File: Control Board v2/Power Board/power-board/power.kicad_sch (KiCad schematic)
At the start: 14 parts, among them J1 1366005, J6 Conn_01x04, J7 Conn_01x02, SW1 SW_SPST

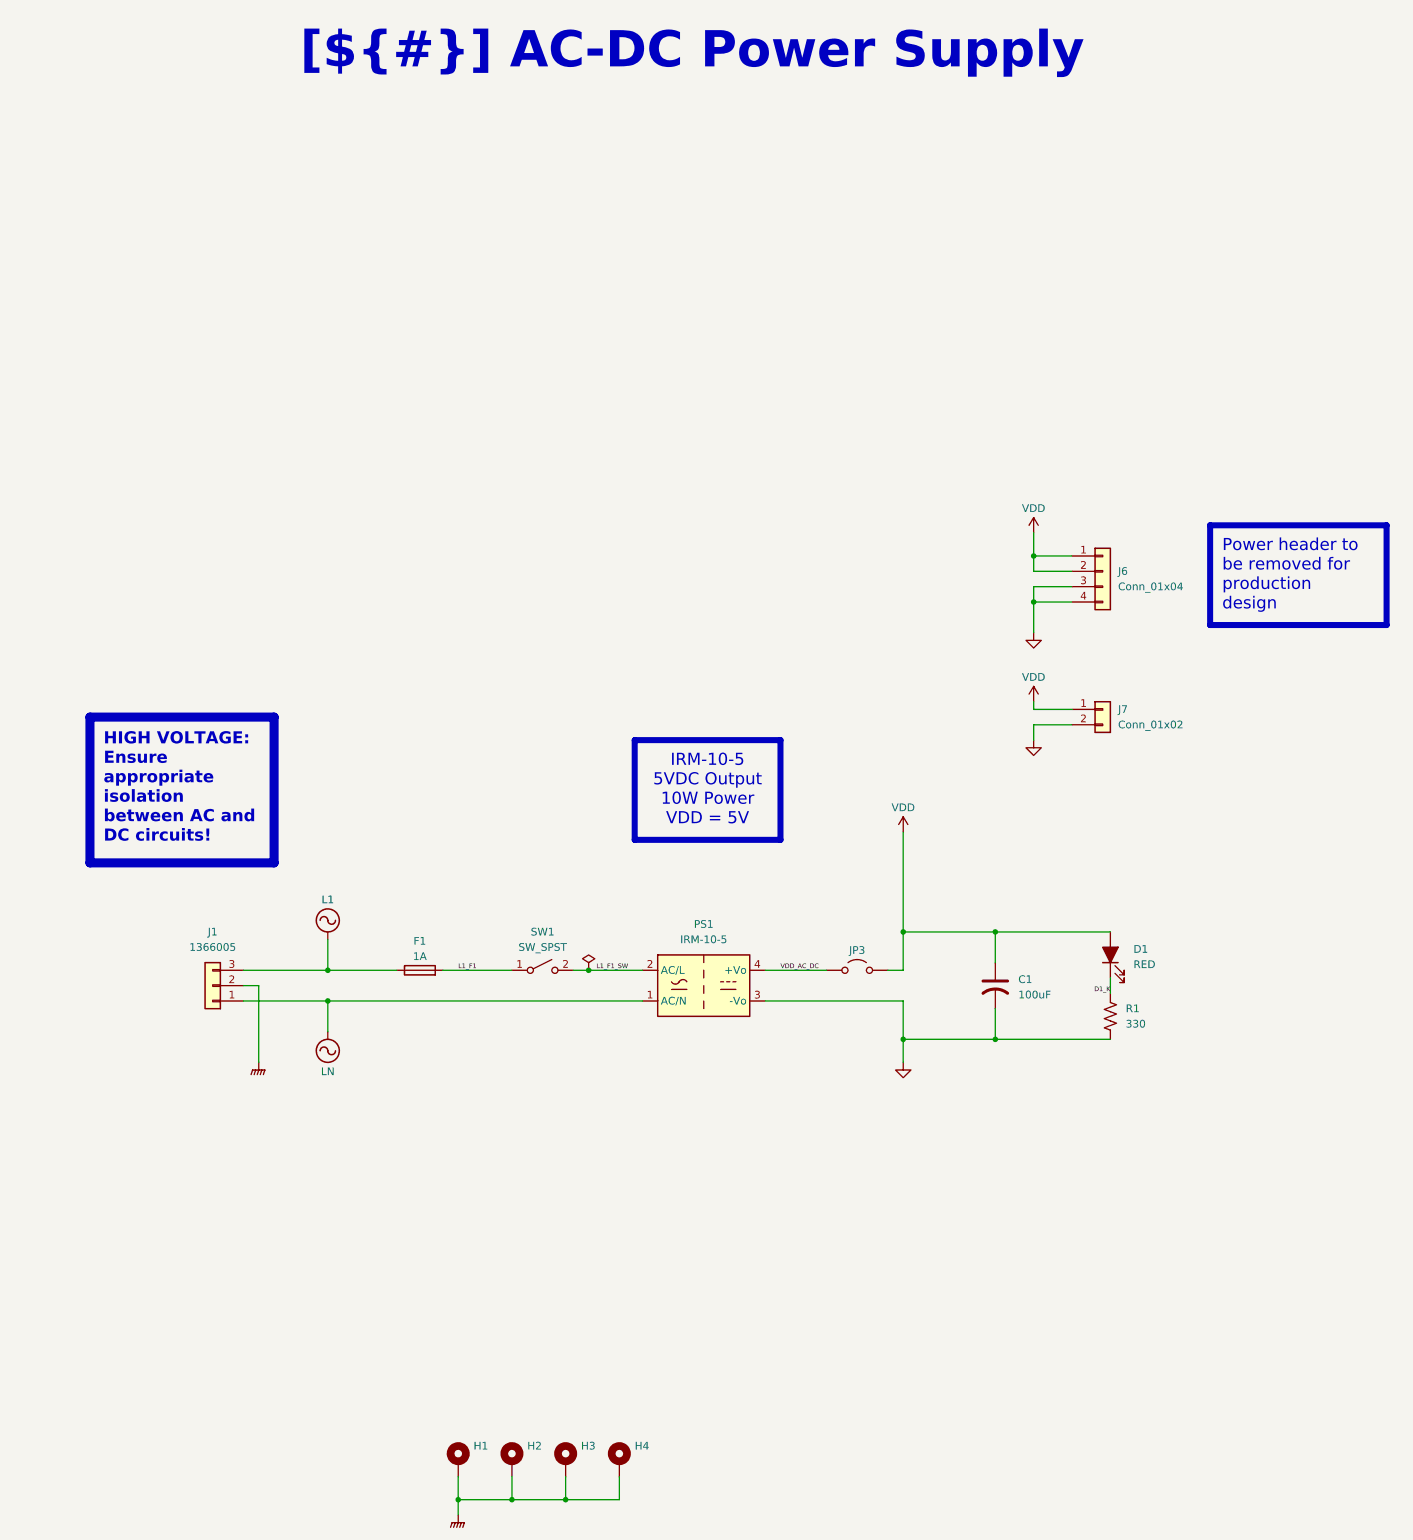
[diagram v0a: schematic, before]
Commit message: schematic mostly done, start board layout
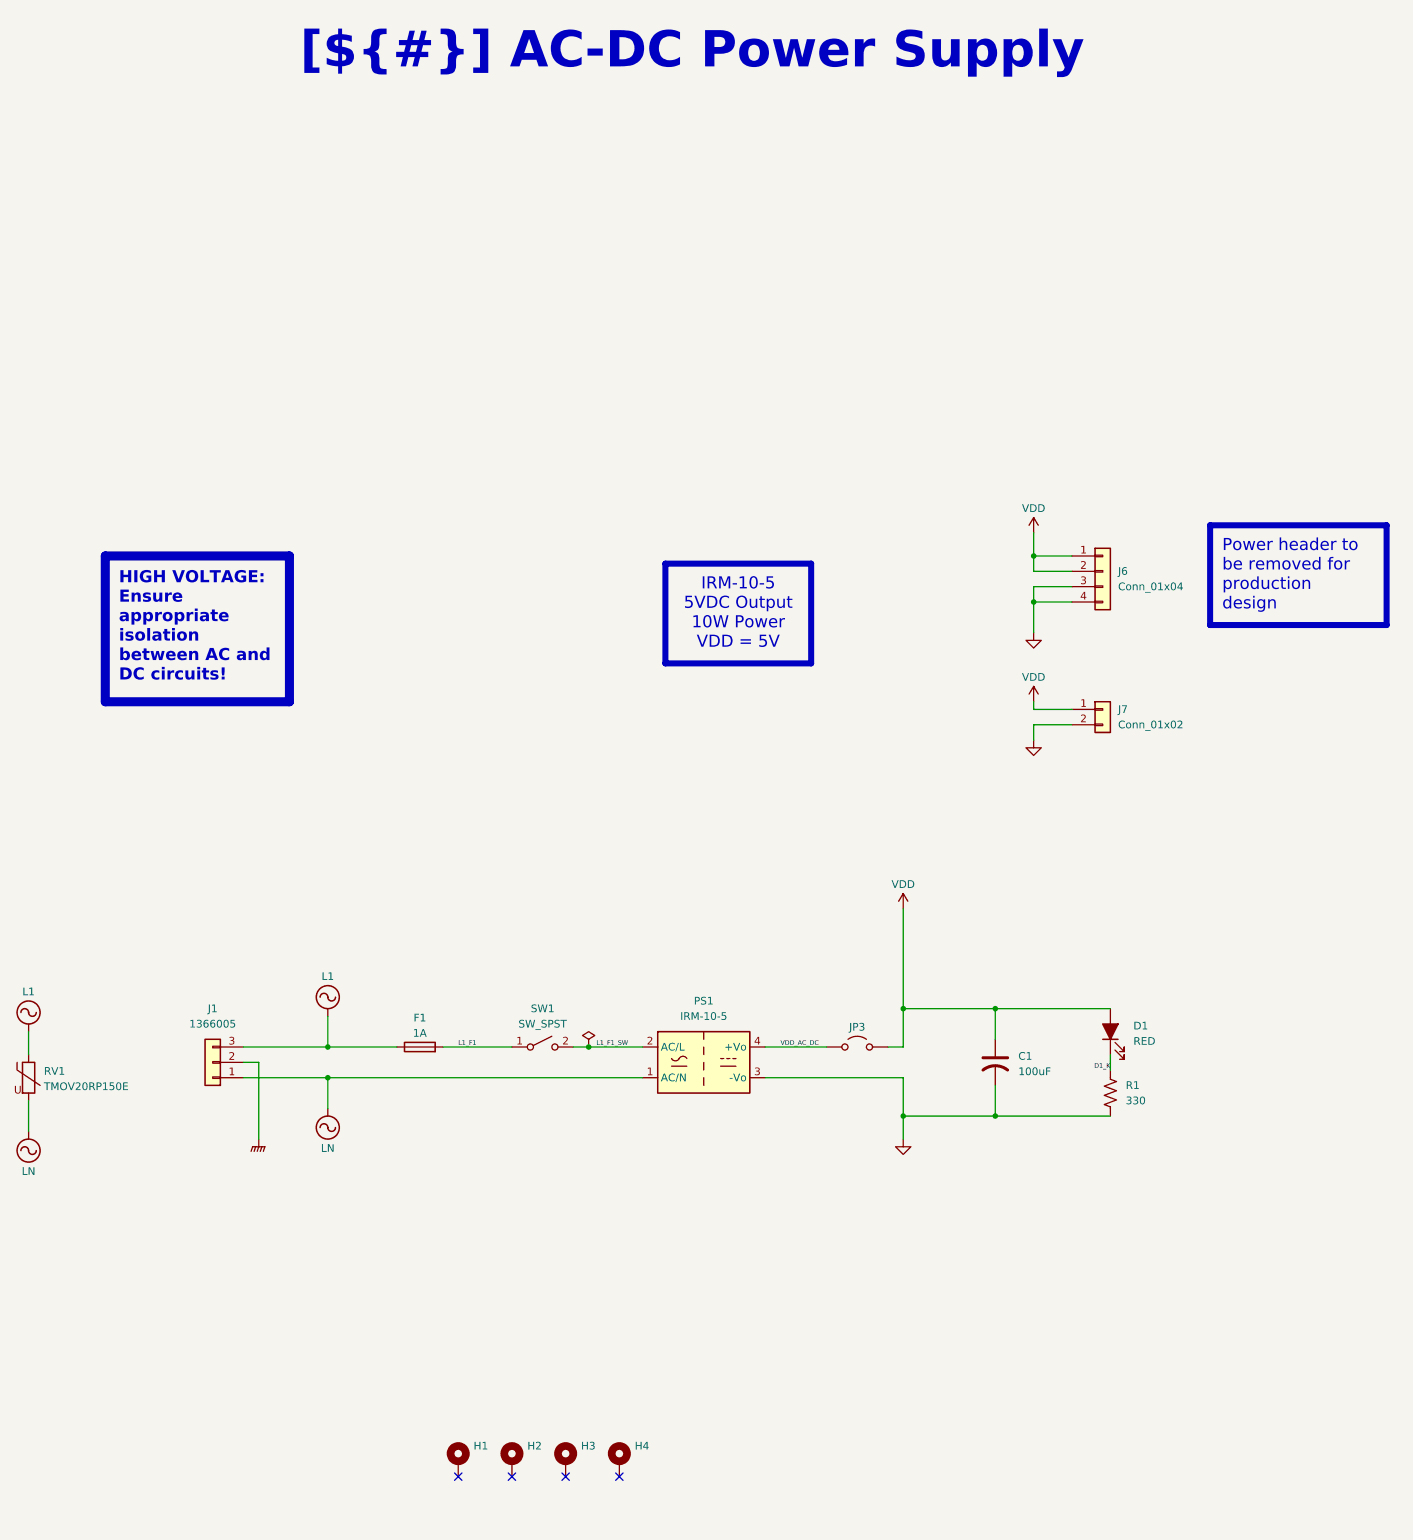
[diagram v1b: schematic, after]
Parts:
- added RV1: TMOV20RP150E, Varistor:RV_Disc_D21.5mm_W8.4mm_P10mm, symbol Device:Varistor
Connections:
- net GNDPWR: no longer H1.1, H2.1, H3.1, H4.1
- net L1: now also RV1.1
- net LN: now also RV1.2
- no-connect marks 0 -> 4
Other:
- moved on the sheet: C1, D1, F1, J1, JP3, PS1, R1, SW1

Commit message: pcb design
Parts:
- F1: footprint Fuse:Fuseholder_Clip-5x20mm_Bel_FC-203-22_Lateral_P17.80x5.00mm_D1.17mm_Horizontal -> Fuse:Fuseholder_Clip-5x20mm_Littelfuse_100_Inline_P20.50x4.60mm_D1.30mm_Horizontal
- RV1: footprint Varistor:RV_Disc_D21.5mm_W8.4mm_P10mm -> TMOV20RP150E:TMOV20RP150E
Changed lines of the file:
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@@
 			)
 		)
-		(property "Footprint" "Fuse:Fuseholder_Clip-5x20mm_Bel_FC-203-22_Lateral_P17.80x5.00mm_D1.17mm_Horizontal"
+		(property "Footprint" "Fuse:Fuseholder_Clip-5x20mm_Littelfuse_100_Inline_P20.50x4.60mm_D1.30mm_Horizontal"
 			(at 165.1 188.468 90)
 			(effects
@@
 			)
 		)
-		(property "Footprint" "Varistor:RV_Disc_D21.5mm_W8.4mm_P10mm"
+		(property "Footprint" "TMOV20RP150E:TMOV20RP150E"
 			(at 98.552 191.77 90)
 			(effects

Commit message: PCB layout is generally complete
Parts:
- removed J6: Conn_01x04, Connector_PinHeader_2.54mm:PinHeader_1x04_P2.54mm_Vertical, symbol Connector_Generic:Conn_01x04
- H1, H2, H3, H4: footprint MountingHole:MountingHole_2.7mm_M2.5_Pad_Via -> MountingHole:MountingHole_2.5mm
